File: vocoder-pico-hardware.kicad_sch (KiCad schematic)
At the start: 42 parts, among them J1 Conn_02x05_Odd_Even, J2 AudioJack3_SwitchTR, SW1 SW_Push, SW2 SW_Push, U1 TL072, U2 LM7805_TO220, U3 PCM5100A

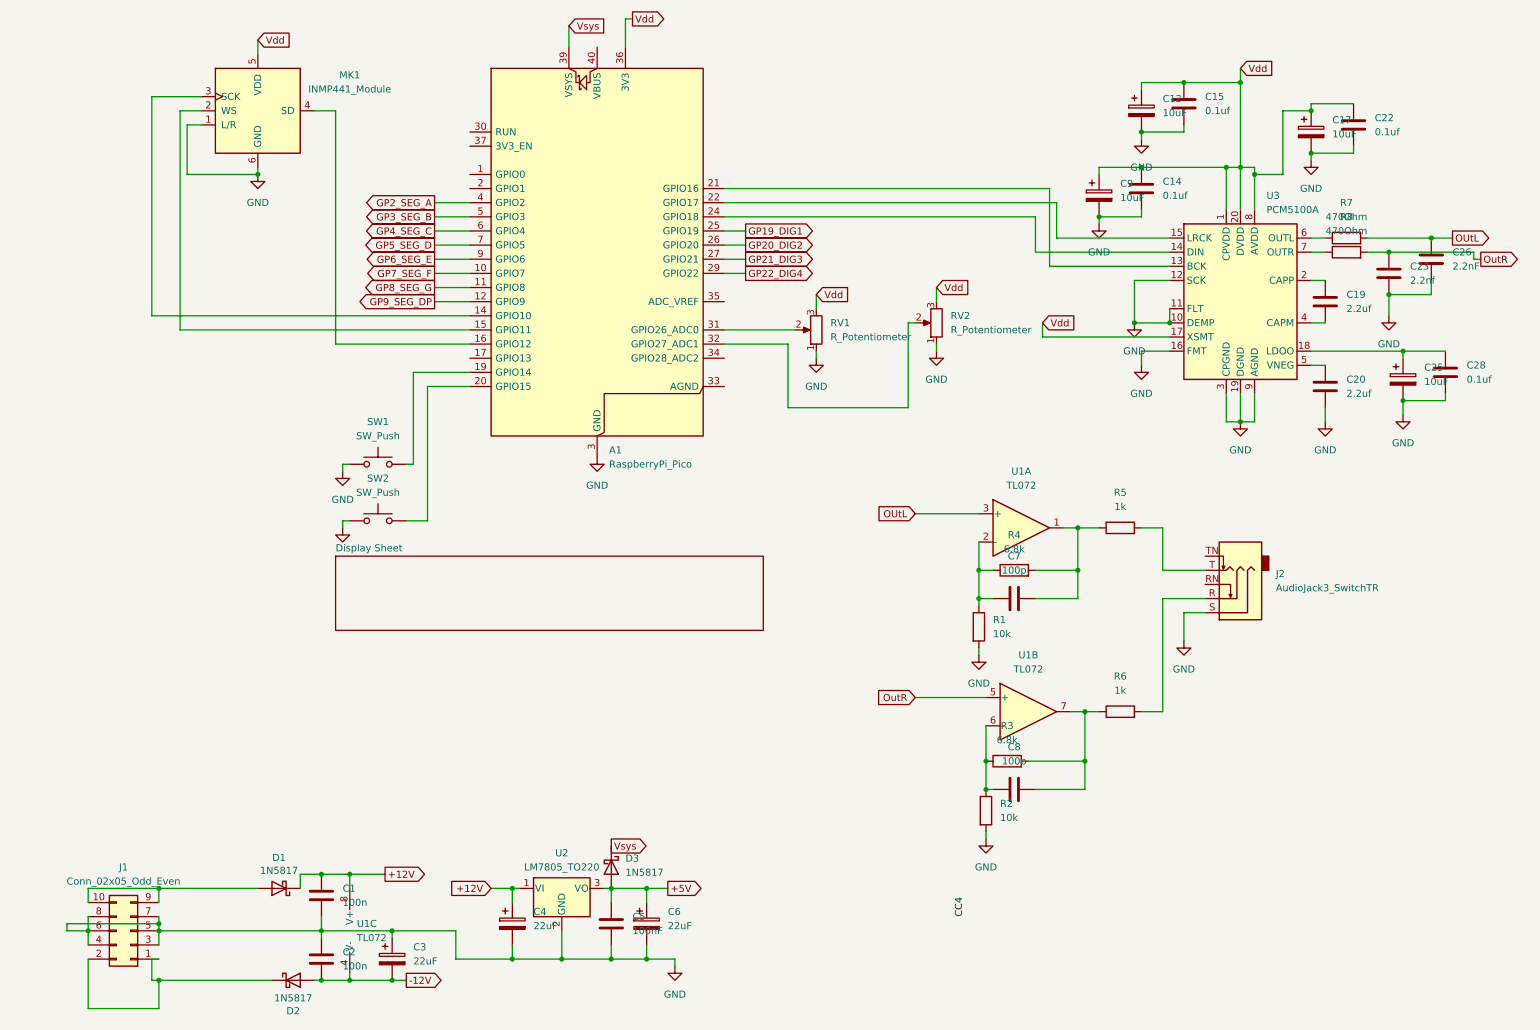
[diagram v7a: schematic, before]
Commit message: implement input stage
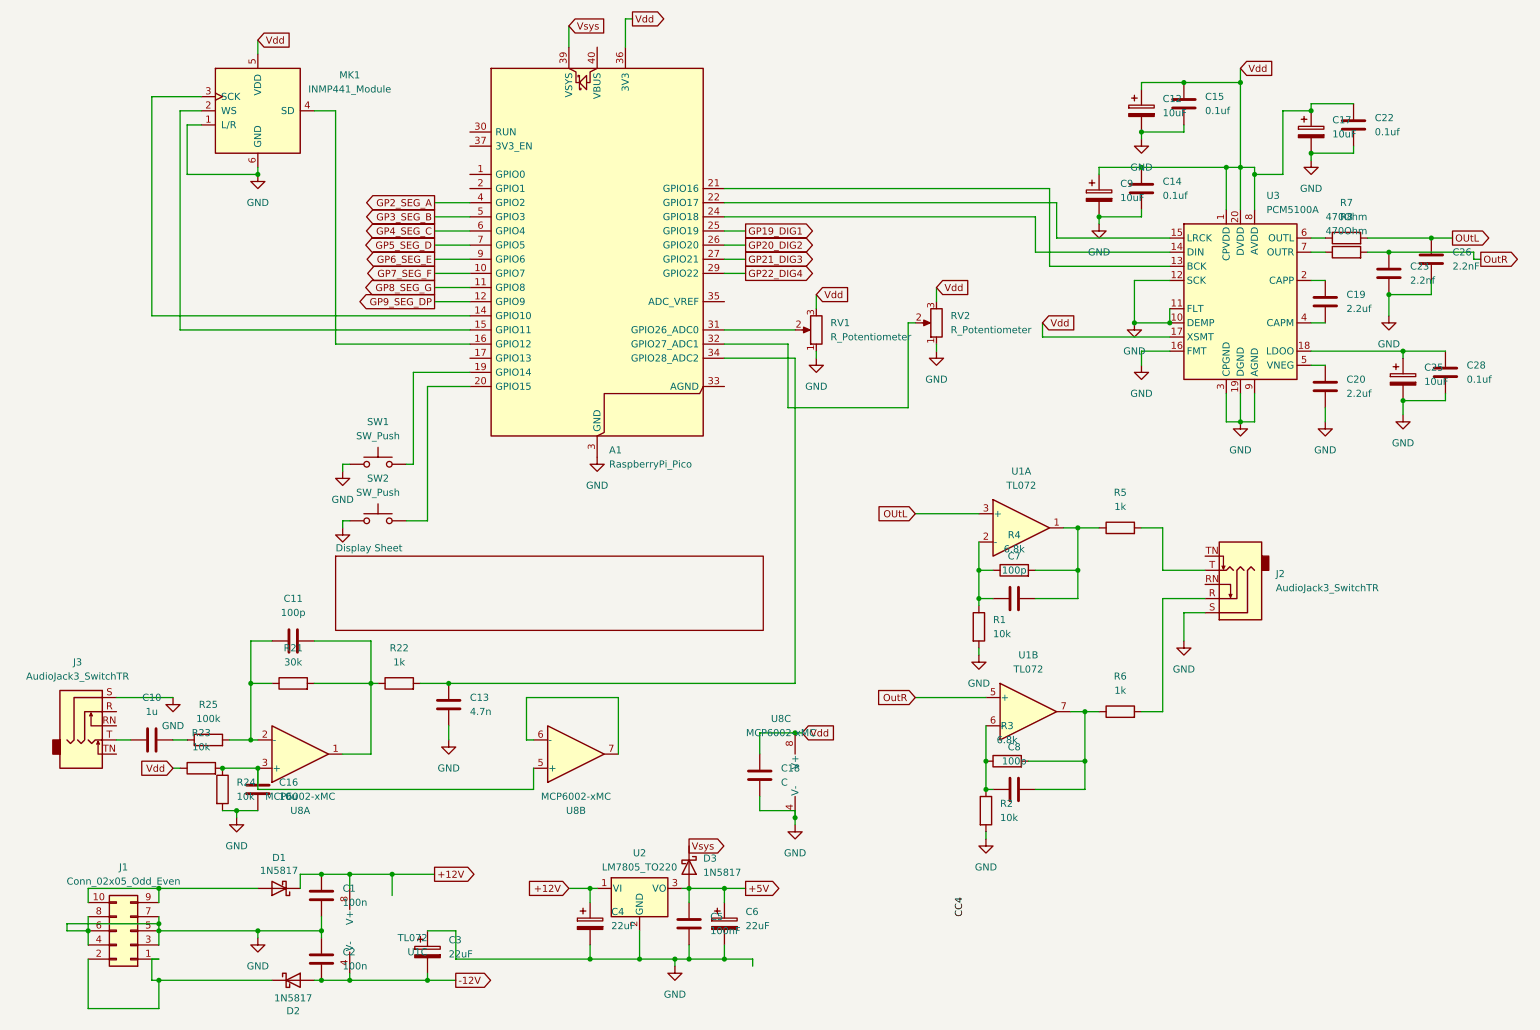
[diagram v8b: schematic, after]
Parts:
- added C10: 1u, symbol Device:C
- added C11: 100p, symbol Device:C
- added C13: 4.7n, symbol Device:C
- added C16: 10u, symbol Device:C
- added C18: C, symbol Device:C
- added J3: AudioJack3_SwitchTR, symbol Connector_Audio:AudioJack3_SwitchTR
- added R21: 30k, symbol Device:R
- added R22: 1k, symbol Device:R
- added R23, R24: 10k, symbol Device:R
- added R25: 100k, symbol Device:R
- added U8: MCP6002-xMC, Package_DFN_QFN:DFN-8-1EP_3x2mm_P0.5mm_EP1.75x1.45mm, symbol Amplifier_Operational:MCP6002-xMC
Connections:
- net GND: now also C13.2, C16.2, C18.2, J3.S, R24.2, U8.4 (V-), U8.9 (V-)
- net Vdd: now also C18.1, R23.1, U8.8 (V+)
- net at A1.34 (GPIO28_ADC2): now also C13.1, R22.2
- new net: C11.2, R21.2, R22.1, U8.1
- new net: C10.1, J3.T
- new net: C10.2, R25.1
- new net: C16.1, R23.2, R24.1, U8.3 (+), U8.5 (+)
- new net: C11.1, R21.1, R25.2, U8.2 (-)
- new net: U8.6 (-), U8.7
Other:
- moved on the sheet: C3, C4, C5, C6, D3, U2
